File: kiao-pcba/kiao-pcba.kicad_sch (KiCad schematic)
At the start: 20 parts, among them J1 USB_C_Receptacle_USB2.0, SW1 BOOT, U1 STM32F072CBT6, U3 xiao_drop-in_gpio_usb_no_cuto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, U4 XC6206PxxxMR-Regulator_Linear, U5 PRTR5V0U2X

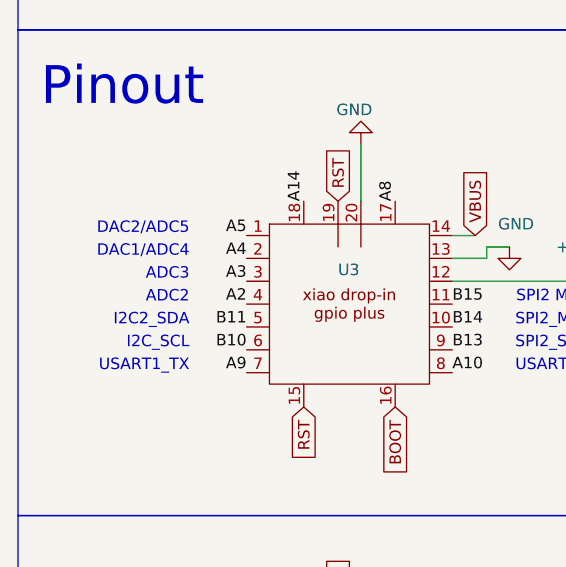
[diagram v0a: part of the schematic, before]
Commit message: Changes pinout, half-panel, gerbers. Proto'd
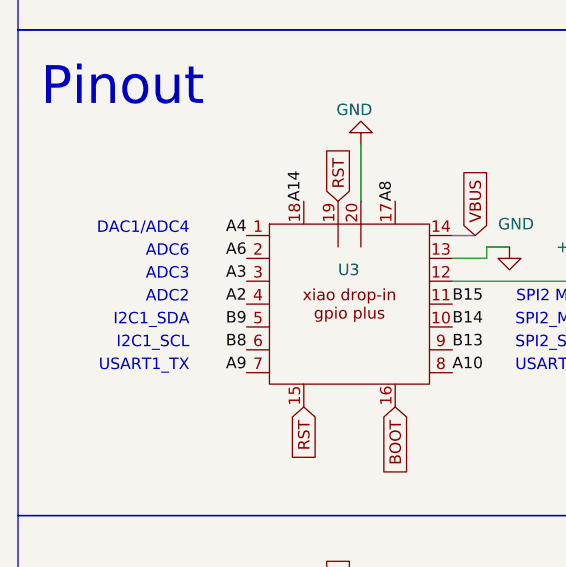
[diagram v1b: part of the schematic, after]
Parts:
- TP1: footprint TestPoint:TestPoint_Pad_D1.0mm -> TestPoint:TestPoint_THTPad_D1.0mm_Drill0.5mm
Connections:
- net A4: now also U3.1; no longer U3.2
- net A5: no longer U3.1
- net A6: now also U3.2
- net B10: no longer U3.6
- net B11: no longer U3.5
- net B8: now also U3.6
- net B9: now also U3.5
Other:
- note added: "ADC6"
- note added: "I2C1_SCL"
- note added: "I2C1_SDA"
- note removed: "DAC2/ADC5"
- note removed: "I2C2_SDA"
- note removed: "I2C_SCL"
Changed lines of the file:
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@@
     (effects (font (size 1.27 1.27)) (justify right bottom))
   )
-  (text "I2C2_SDA" (at 31.75 131.445 0)
+  (text "I2C1_SDA" (at 31.75 131.445 0)
     (effects (font (size 1.27 1.27)) (justify right bottom))
   )
@@
     (effects (font (size 1.27 1.27)) (justify right bottom))
   )
-  (text "DAC1/ADC4" (at 31.75 123.825 0)
+  (text "DAC1/ADC4" (at 31.75 121.285 0)
     (effects (font (size 1.27 1.27)) (justify right bottom))
   )
@@
     (effects (font (size 4.2 4.2)) (justify left bottom))
   )
-  (text "DAC2/ADC5" (at 31.75 121.285 0)
+  (text "ADC6" (at 31.75 123.825 0)
     (effects (font (size 1.27 1.27)) (justify right bottom))
   )
@@
     (effects (font (size 1.27 1.27)) (justify left bottom))
   )
-  (text "I2C_SCL" (at 31.75 133.985 0)
+  (text "I2C1_SCL" (at 31.75 133.985 0)
     (effects (font (size 1.27 1.27)) (justify right bottom))
   )
@@
     (effects (font (size 1.27 1.27)) (justify right bottom))
   )
-  (label "B11" (at 38.1 131.445 180) (fields_autoplaced)
-    (effects (font (size 1.27 1.27)) (justify right bottom))
-  )
   (label "C13" (at 201.93 52.705 180) (fields_autoplaced)
     (effects (font (size 1.27 1.27)) (justify right bottom))
@@
     (effects (font (size 1.27 1.27)) (justify right bottom))
   )
+  (label "B8" (at 38.1 133.985 180) (fields_autoplaced)
+    (effects (font (size 1.27 1.27)) (justify right bottom))
+  )
   (label "A13" (at 240.03 67.945 0) (fields_autoplaced)
     (effects (font (size 1.27 1.27)) (justify left bottom))
@@
     (effects (font (size 1.27 1.27)) (justify right bottom))
   )
-  (label "A5" (at 38.1 121.285 180) (fields_autoplaced)
+  (label "A6" (at 38.1 123.825 180) (fields_autoplaced)
     (effects (font (size 1.27 1.27)) (justify right bottom))
   )
@@
     (effects (font (size 1.27 1.27)) (justify left bottom))
   )
-  (label "A4" (at 38.1 123.825 180) (fields_autoplaced)
+  (label "A4" (at 38.1 121.285 180) (fields_autoplaced)
+    (effects (font (size 1.27 1.27)) (justify right bottom))
+  )
+  (label "B9" (at 38.1 131.445 180) (fields_autoplaced)
     (effects (font (size 1.27 1.27)) (justify right bottom))
   )
   (label "B2" (at 202.565 67.945 180) (fields_autoplaced)
-    (effects (font (size 1.27 1.27)) (justify right bottom))
-  )
-  (label "B10" (at 38.1 133.985 180) (fields_autoplaced)
     (effects (font (size 1.27 1.27)) (justify right bottom))
   )
@@
       (effects (font (size 1.27 1.27)) (justify left))
     )
-    (property "Footprint" "TestPoint:TestPoint_Pad_D1.0mm" (at 111.125 179.705 0)
-      (effects (font (size 1.27 1.27)) hide)
-    )
+    (property "Footprint" "TestPoint:TestPoint_THTPad_D1.0mm_Drill0.5mm" (at 111.125 179.705 0)
+      (effects (font (size 1.27 1.27)) hide)
+    )
